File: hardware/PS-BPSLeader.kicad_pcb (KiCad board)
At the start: 4 copper layers, 100 x 100 mm, 386 parts, among them IC1 TCAN3413DR, IC2 TCAN3413DR, IC3 CYPD3177-24LQXQ, IC4 BQ79600PWRQ1, IC5 LM74502DDFR, IC6 TCAN3413DR, IC7 TPS552872RYQR, J1 USB_C_Receptacle_USB2.0_16P, J10 Low SIde Conn, J11 SWD_Header, J12 SWD, J13 USB_C_Receptacle_USB2.0_16P, J14 Conn_01x02, J15 Contactor Connector, J16 Contactor Connector, J17 Contactor Connector, J2 ELCON CAN DEBUG, J3 ELCON CAN, J4 Conn_02x06_Counter_Clockwise, J5 CAR CAN IN, J6 CAR CAN OUT, J7 BPS CAN DEBUG, J8 BPS CAN, J9 High Side Conn, Q1 SQ2315CES-T1_GE3, Q10 SI7997DP-T1-GE3, Q11 SI7997DP-T1-GE3, Q12 IRLML0030, Q13 PSMN012-100YS, Q14 PSMN012-100YS, Q2 SQ2315CES-T1_GE3, Q3 SQ2315CES-T1_GE3, Q4 IRLML0030, Q5 IRLML0030, Q6 IRLML0030, Q7 IRLML0030, Q8 IRLML0030, Q9 IRLML0030, SW1 SW_SPDT, SW2 BOOT Switch, SW3 RESET Button, T1 HMU1228NL, T2 HMU1228NL, U1 STM32G473VETx, U10 MCP1826S, U11 TPS2117DRLR, U12 LMR51635XDDCR, U13 PESD5V0L2BT, U14 PESD5V0L2BT, U15 TPS2117DRLR, U16 MCP1826S, U17 TPS2121RUXR, U18 CDSOT23-T24CAN, U2 CDSOT23-T24CAN, U3 CDSOT23-T24CAN, U4 ESP32-C6-MINI-1, U5 DRV110APWR, U6 TPS2121RUXR, U7 DRV110APWR, U8 DRV110APWR, U9 EMC2305-1-AP-TR, Y1 Crystal

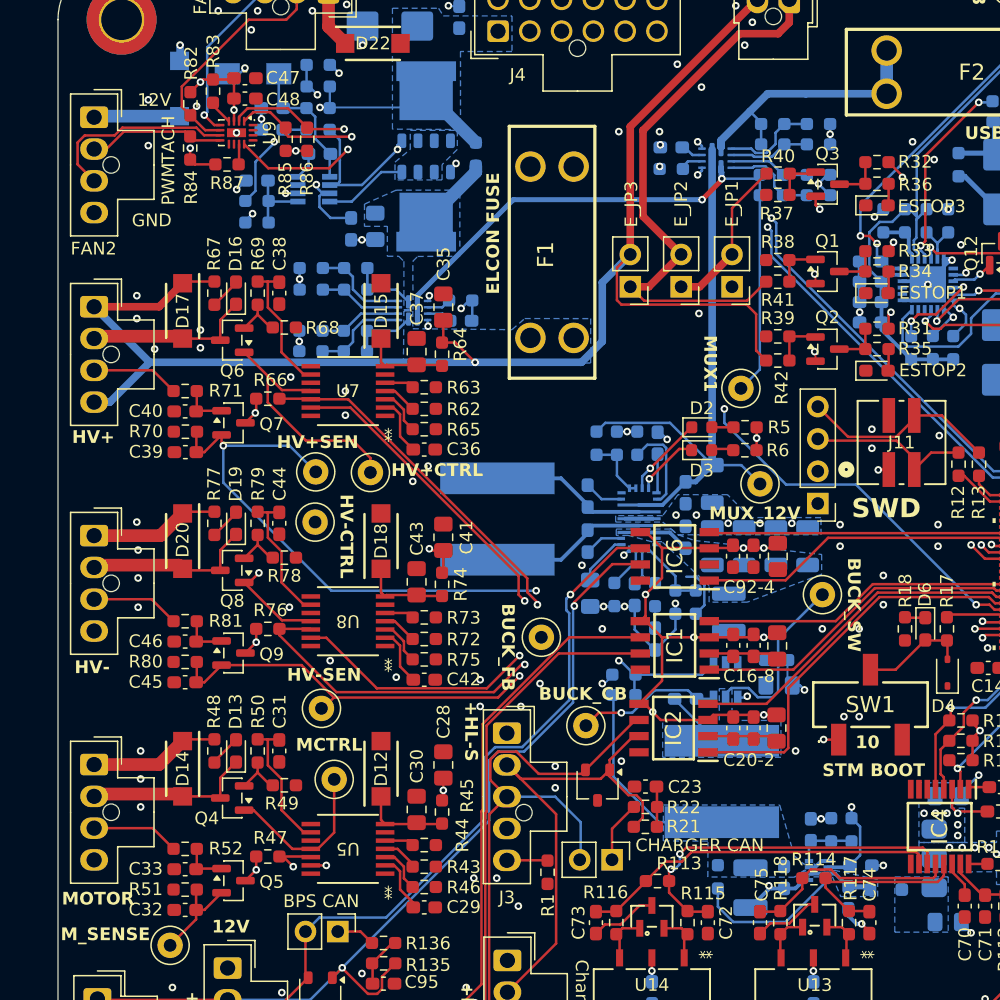
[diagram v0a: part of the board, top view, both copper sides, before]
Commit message: fixed fan chip footprint and buck output capacitors
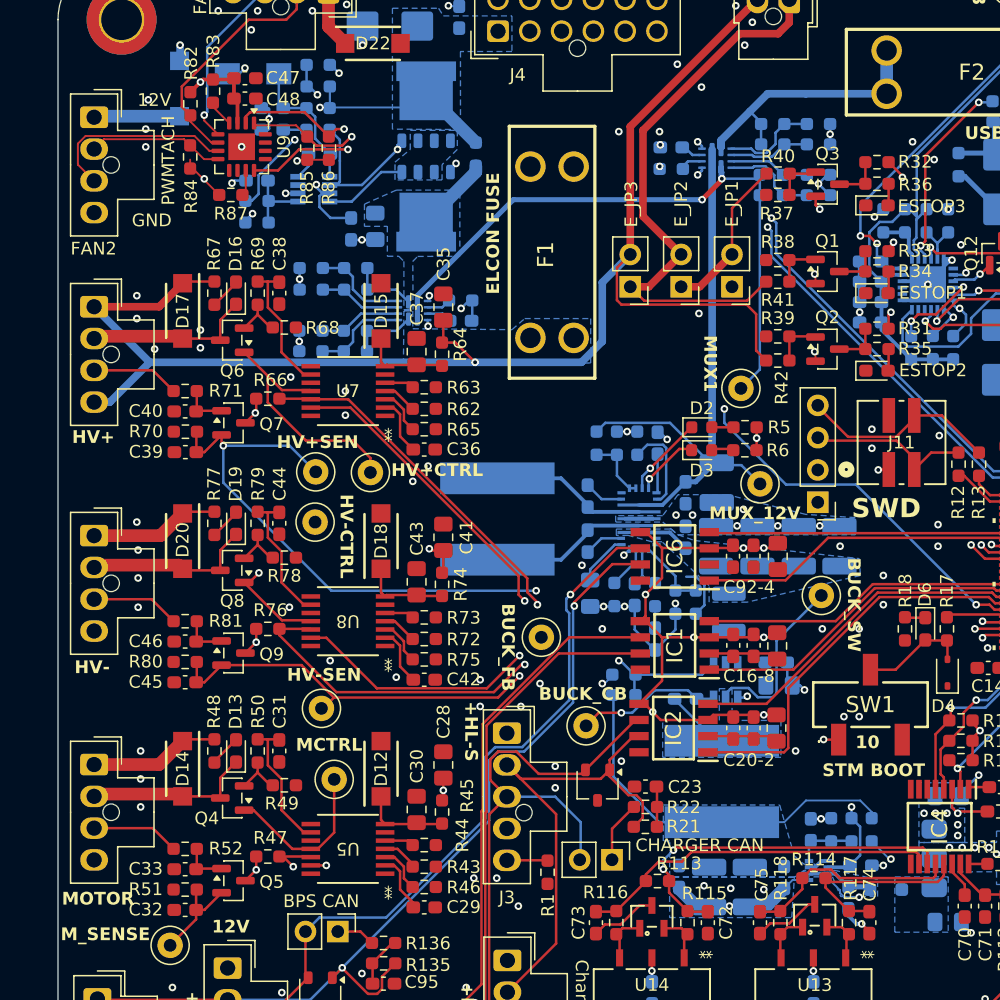
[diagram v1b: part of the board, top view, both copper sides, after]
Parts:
- added C108: 4.7u, Capacitor_SMD:C_0603_1608Metric_Pad1.08x0.95mm_HandSolder, B.Cu at (173.8, 107.4)
- added C109: 22u, Capacitor_SMD:C_1210_3225Metric_Pad1.33x2.70mm_HandSolder, B.Cu at (176.2, 108.2)
- C101, C102, C103, C105, C97: footprint Capacitor_SMD:C_1206_3216Metric -> Capacitor_SMD:C_1210_3225Metric_Pad1.33x2.70mm_HandSolder
- C58: value 47u -> 22u
- U9: footprint Package_DFN_QFN:QFN-16-1EP_1.8x2.6mm_P0.4mm_EP0.7x1.5mm -> Package_DFN_QFN:Texas_RGV0016A_VQFN-16-1EP_4x4mm_P0.65mm_EP2.1x2.1mm
- moved R125 12.7 mm to (189.0, 103.7)
- moved C105 2.50 mm to (186.4, 81.4)
- moved R87 2.42 mm to (138.6, 53.8)
- moved R86 1.84 mm to (146.3, 50.1)
- moved R85 1.84 mm to (144.6, 50.1)
- moved C103 1.80 mm to (183.2, 81.4)
- moved U9 1.17 mm to (139.4, 50.0)
- moved C102 1.05 mm to (180.0, 81.4)
- moved R84 0.70 mm to (135.4, 50.8)
- moved C97 0.36 mm to (176.8, 76.4)
- moved C101 0.30 mm to (176.8, 81.4)
- moved C56 0.20 mm to (181.5, 90.5)
- moved TP14 0.11 mm to (185.0, 85.3)
- moved J12 0.10 mm to (184.7, 77.9)
- moved C58 0.07 mm to (179.4, 108.2)
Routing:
- net /Power/5V_BUCK: track 18.1 -> 31.5 mm
- net GND: track 137.3 -> 143.3 mm, vias 217 -> 221
- net Net-(U15-ST): track 11.9 -> 9.35 mm, vias 0 -> 2
- net +3.3V: track 103.6 -> 105.4 mm, vias 36 -> 35
- net /FAN_ALERT: track 82.9 -> 81.4 mm
- net /FAN_SDA: track 81.3 -> 80.2 mm
- net /BMS/COMLN: track 28.0 -> 28.6 mm
- net /Fan/CLK_PULLUP: track 1.50 -> 2.04 mm
- net /Fan/FAN_1_TACH: track 19.4 -> 19.0 mm, vias 1 -> 0
